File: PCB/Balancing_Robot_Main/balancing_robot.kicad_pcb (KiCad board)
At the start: 4 copper layers, 120 x 50 mm, 56 parts, among them J1 Screw_Terminal_01x02, J2 USB_C_Receptacle_USB2.0, J3 Conn_01x05, J4 Conn_01x05, J5 Conn_01x05, J6 Conn_01x05, J7 Conn_01x05, J8 Conn_01x05, J9 Conn_01x05, Q1 UMH3N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

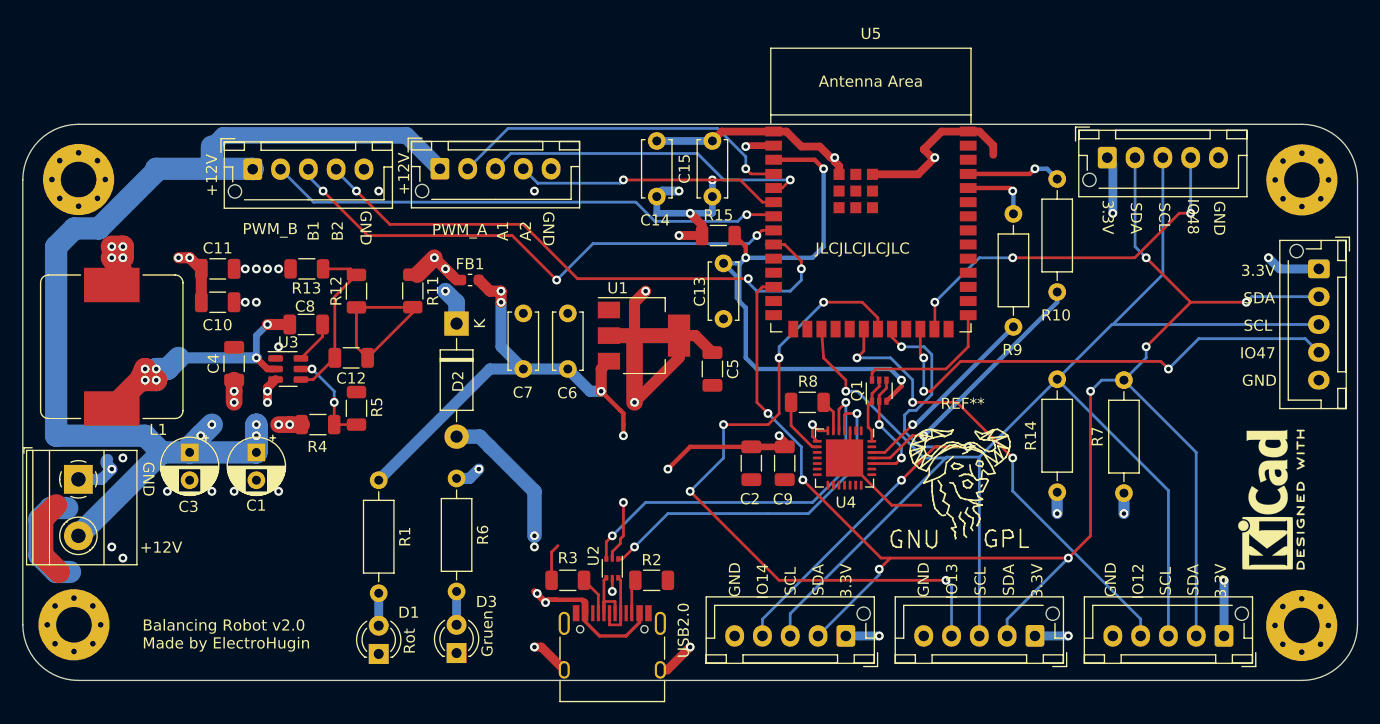
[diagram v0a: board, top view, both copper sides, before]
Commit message: Updated PCB Main and MotorBridge with Pins for Encoder
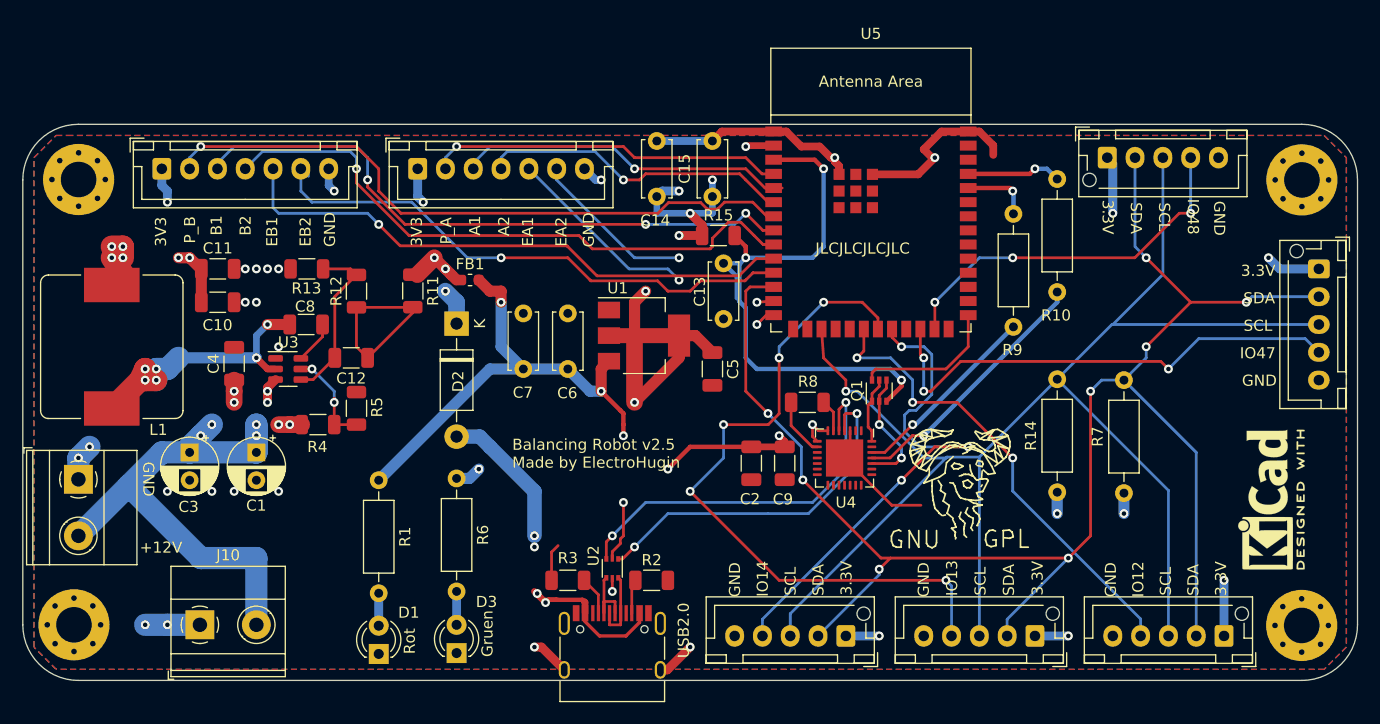
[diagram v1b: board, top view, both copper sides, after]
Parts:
- added J10: Screw_Terminal_01x02, TerminalBlock_Phoenix:TerminalBlock_Phoenix_MKDS-1,5-2-5.08_1x02_P5.08mm_Horizontal, F.Cu at (108.9, 113.0)
- J8, J9: value Conn_01x05 -> Conn_01x07; footprint Connector_JST:JST_XH_B5B-XH-AM_1x05_P2.50mm_Vertical -> Connector_JST:JST_XH_B7B-XH-A_1x07_P2.50mm_Vertical
- moved J9 8.17 mm to (105.5, 72.0)
- moved J8 2.00 mm to (128.5, 72.0)
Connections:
- J8 pad 1: +12VA -> +3.3V
- J8 pad 5: GND -> /EA1
- J9 pad 1: +12VA -> +3.3V
- J9 pad 5: GND -> /EB1
- U5 pad 10: unconnected-(U5-GPIO17/U1TXD/ADC2_CH6-Pad10) -> /EB1
- U5 pad 11: unconnected-(U5-GPIO18/U1RXD/ADC2_CH7/CLK_OUT3-Pad11) -> /EB2
- U5 pad 13: unconnected-(U5-GPIO19/U1RTS/ADC2_CH8/CLK_OUT2/USB_D--Pad13) -> /EA2
- U5 pad 14: unconnected-(U5-GPIO20/U1CTS/ADC2_CH9/CLK_OUT1/USB_D+-Pad14) -> /EA1
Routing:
- net +3.3V: track 241.0 -> 294.6 mm, vias 15 -> 17
- net +12VA: track 116.0 -> 64.2 mm
- net /EB1: track 0.00 -> 51.7 mm, vias 0 -> 1
- net /EB2: track 0.00 -> 49.5 mm, vias 0 -> 1
- net /EA1: track 0.00 -> 28.1 mm, vias 0 -> 2
- net /EA2: track 0.00 -> 25.2 mm, vias 0 -> 2
- net /PWM_B: track 46.5 -> 59.2 mm
- net GND: track 78.9 -> 70.2 mm
- net /B1: track 48.2 -> 56.6 mm
- net /A2: track 24.0 -> 28.1 mm
- net /B2: track 52.5 -> 56.1 mm, vias 3 -> 1
- net /SDA: track 147.2 -> 148.7 mm
- net /PWM_A: track 31.3 -> 31.9 mm
- net /A1: track 29.9 -> 30.4 mm
- net +5V: vias 8 -> 7
- added copper zone on B.Cu, net GND
- added copper zone on F.Cu, net GND
- added copper zone on In1.Cu, net GND
- added copper zone on In2.Cu, net GND
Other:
- board text added: "3V3"
- board text added: "Balancing Robot v2.5 Made by ElectroHugin"
- board text added: "EA1"
- board text added: "EA2"
- board text added: "EB1"
- board text added: "EB2"
- board text added: "P_A"
- board text added: "P_B"
- board text removed: "Balancing Robot v2.0 Made by ElectroHugin"
- board text removed: "PWM_A"
- board text removed: "PWM_B"

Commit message: Converted all vias to through-hole
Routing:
- net +5V: track 78.9 -> 79.6 mm

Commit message: Added Visuals
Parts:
- removed R11: 49.9, Resistor_SMD:R_1206_3216Metric
- removed R4: 511k, Resistor_SMD:R_1206_3216Metric
- removed R5: 105k, Resistor_SMD:R_1206_3216Metric
- removed U3: TPS54302, Package_TO_SOT_SMD:SOT-23-6
- added U6: TPS62933, Package_TO_SOT_SMD:SOT-583-8, F.Cu at (108.5, 87.0)
- C10: value 22u -> 100n
- C11: value 22u -> 47p
- C12: value 75p -> 47u
- C4: value 0.1u -> 33n
- C8: value 0.1u -> 100n
- L1: footprint Inductor_SMD:L_Bourns_SRP1245A -> Inductor_SMD:L_Bourns_SRR1208_12.7x12.7mm
- R12: value 100k -> 52k3
- R13: value 13k3 -> 10k
- moved J10 34.7 mm to (98.2, 80.0), turned to -90 degrees
- moved C12 20.6 mm to (113.5, 107.5)
- moved L1 20.0 mm to (118.0, 98.5), turned to -90 degrees
- moved C1 13.3 mm to (103.0, 90.0)
- moved FB1 12.4 mm to (127.0, 92.8), turned to 90 degrees
- moved C3 11.3 mm to (97.0, 95.0), turned to 0 degrees
- moved R13 9.05 mm to (109.5, 81.5), turned to 90 degrees
- moved R12 7.64 mm to (115.5, 81.5), turned to -90 degrees
- moved C8 6.69 mm to (112.5, 89.0), turned to -90 degrees
- moved C10 5.41 mm to (105.5, 86.0), turned to -90 degrees
- moved C4 4.06 mm to (112.5, 85.5), turned to 180 degrees
- moved C11 2.04 mm to (112.5, 81.5), turned to -90 degrees
- moved D1 1.50 mm to (126.5, 115.6)
- moved R1 1.50 mm to (126.5, 100.0)
- moved J1 1.00 mm to (98.0, 100.9)
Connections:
- net Net-(U3-SW) renamed /SW
- C10 pad 1: +5VP -> GND
- C10 pad 2: GND -> +12VA
- C11 pad 2: GND -> Net-(U6-FB)
- C12 pad 1: Net-(C12-Pad1) -> +5VP
- C12 pad 2: Net-(U3-FB) -> GND
- C4 pad 1: +12VA -> GND
- C4 pad 2: GND -> Net-(U6-SS)
- J1 pad 1: GND -> +12VA
- J1 pad 2: +12VA -> GND
- R12 pad 1: Net-(C12-Pad1) -> +5VP
- R12 pad 2: Net-(U3-FB) -> Net-(U6-FB)
- R13 pad 1: Net-(U3-FB) -> Net-(U6-FB)
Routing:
- net +12VA: track 64.2 -> 28.8 mm, vias 10 -> 1
- net +5VP: track 58.5 -> 83.2 mm, vias 9 -> 3
- net Net-(C12-Pad1): track 16.3 -> 0.00 mm
- net Net-(U3-FB): track 15.4 -> 0.00 mm
- net Net-(U3-EN): track 9.60 -> 0.00 mm, vias 2 -> 0
- net Net-(U6-FB): track 0.00 -> 9.44 mm
- net +5V: track 79.6 -> 74.2 mm, vias 7 -> 8
- net /SW: track 24.7 -> 19.7 mm, vias 6 -> 0
- net GND: track 70.2 -> 74.8 mm, vias 22 -> 88
- net Net-(U6-SS): track 0.00 -> 2.31 mm
- net Net-(U6-BST): track 3.93 -> 3.36 mm
- added copper zone on F.Cu, net +5VP
- added copper zone on F.Cu, net /SW
- removed copper zone on In2.Cu, net +12VA
- removed copper zone on In2.Cu, net +5VP
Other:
- board text added: "Balancing Robot v3.0 Made by ElectroHugin"
- board text removed: "Balancing Robot v2.5 Made by ElectroHugin"
